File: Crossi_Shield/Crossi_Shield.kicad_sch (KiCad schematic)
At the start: 1 part, among them J2 10090926-P444VLF

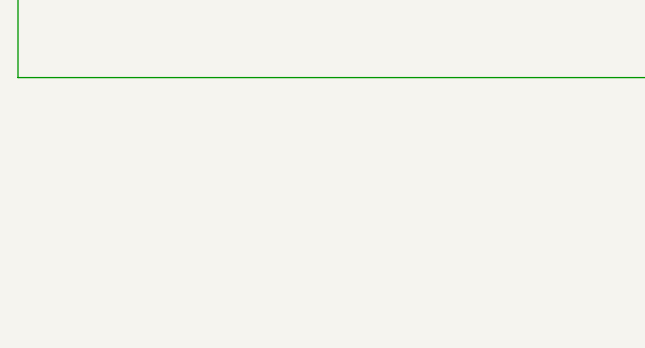
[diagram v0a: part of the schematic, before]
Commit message: add 5V and gnd
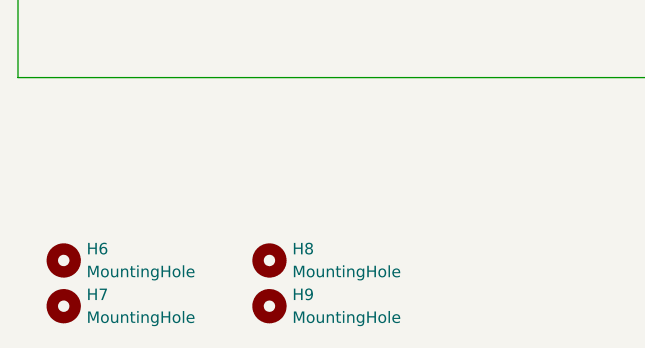
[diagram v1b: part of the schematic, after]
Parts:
- added H6, H7, H8, H9: MountingHole, MountingHole:MountingHole_3.2mm_M3_DIN965_Pad, symbol Mechanical:MountingHole
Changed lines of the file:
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@@
     (effects (font (size 10 10) (thickness 2) bold (color 0 0 255 1)) (justify left bottom))
+  )
+  (symbol (lib_id "Mechanical:MountingHole") (at 40.64 180.34 0) (unit 1)
+    (in_bom yes) (on_board yes) (dnp no) (fields_autoplaced)
+    (property "Reference" "H6" (at 43.18 179.07 0)
+      (effects (font (size 1.27 1.27)) (justify left))
+    )
+    (property "Value" "MountingHole" (at 43.18 181.61 0)
+      (effects (font (size 1.27 1.27)) (justify left))
+    )
+    (property "Footprint" "MountingHole:MountingHole_3.2mm_M3_DIN965_Pad" (at 40.64 180.34 0)
+      (effects (font (size 1.27 1.27)) hide)
+    )
+    (property "Datasheet" "~" (at 40.64 180.34 0)
+      (effects (font (size 1.27 1.27)) hide)
+    )
+    (instances
+      (project "Crossi_Shield"
+        (path "/da1a3662-bd33-45fa-9d2c-eaee6b865c8d"
+          (reference "H6") (unit 1)
+        )
+      )
+    )
+  )
+  (symbol (lib_id "Mechanical:MountingHole") (at 63.5 185.42 0) (unit 1)
+    (in_bom yes) (on_board yes) (dnp no) (fields_autoplaced)
+    (property "Reference" "H9" (at 66.04 184.15 0)
+      (effects (font (size 1.27 1.27)) (justify left))
+    )
+    (property "Value" "MountingHole" (at 66.04 186.69 0)
+      (effects (font (size 1.27 1.27)) (justify left))
+    )
+    (property "Footprint" "MountingHole:MountingHole_3.2mm_M3_DIN965_Pad" (at 63.5 185.42 0)
+      (effects (font (size 1.27 1.27)) hide)
+    )
+    (property "Datasheet" "~" (at 63.5 185.42 0)
+      (effects (font (size 1.27 1.27)) hide)
+    )
+    (instances
+      (project "Crossi_Shield"
+        (path "/da1a3662-bd33-45fa-9d2c-eaee6b865c8d"
+          (reference "H9") (unit 1)
+        )
+      )
+    )
   )
   (symbol (lib_id "power:GND") (at 217.17 128.27 180) (unit 1)
@@
         )
       )
+    )
+  )
+  (symbol (lib_id "Mechanical:MountingHole") (at 40.64 185.42 0) (unit 1)
+    (in_bom yes) (on_board yes) (dnp no) (fields_autoplaced)
+    (property "Reference" "H7" (at 43.18 184.15 0)
+      (effects (font (size 1.27 1.27)) (justify left))
+    )
+    (property "Value" "MountingHole" (at 43.18 186.69 0)
+      (effects (font (size 1.27 1.27)) (justify left))
+    )
+    (property "Footprint" "MountingHole:MountingHole_3.2mm_M3_DIN965_Pad" (at 40.64 185.42 0)
+      (effects (font (size 1.27 1.27)) hide)
+    )
+    (property "Datasheet" "~" (at 40.64 185.42 0)
+      (effects (font (size 1.27 1.27)) hide)
+    )
+    (instances
+      (project "Crossi_Shield"
+        (path "/da1a3662-bd33-45fa-9d2c-eaee6b865c8d"
+          (reference "H7") (unit 1)
+        )
+      )
+    )
+  )
+  (symbol (lib_id "Mechanical:MountingHole") (at 63.5 180.34 0) (unit 1)
+    (in_bom yes) (on_board yes) (dnp no) (fields_autoplaced)
+    (property "Reference" "H8" (at 66.04 179.07 0)
+      (effects (font (size 1.27 1.27)) (justify left))
+    )
+    (property "Value" "MountingHole" (at 66.04 181.61 0)
+      (effects (font (size 1.27 1.27)) (justify left))
+    )
+    (property "Footprint" "MountingHole:MountingHole_3.2mm_M3_DIN965_Pad" (at 63.5 180.34 0)
+      (effects (font (size 1.27 1.27)) hide)
+    )
+    (property "Datasheet" "~" (at 63.5 180.34 0)
+      (effects (font (size 1.27 1.27)) hide)
+    )
+    (instances
+      (project "Crossi_Shield"
+        (path "/da1a3662-bd33-45fa-9d2c-eaee6b865c8d"
+          (reference "H8") (unit 1)
+        )
+      )
